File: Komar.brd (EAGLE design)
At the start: 58 x 58 mm, 108 parts, among them CON1 USB-VERTICAL, CON2 PINHEAD_1X01-2, CON3 CON-4P-TABS-STRAIGHT, CON4 CON-4P-TABS-STRAIGHT, CON5 CON-4P-TABS-STRAIGHT, CON6 CON-4P-TABS-STRAIGHT, CON7 CON-4P-TABS-STRAIGHT, CON8 CON-6P-SM06B, CON9 PINHEAD_1X01-2, IC1 TPD3S014DBVR-SOT23-6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

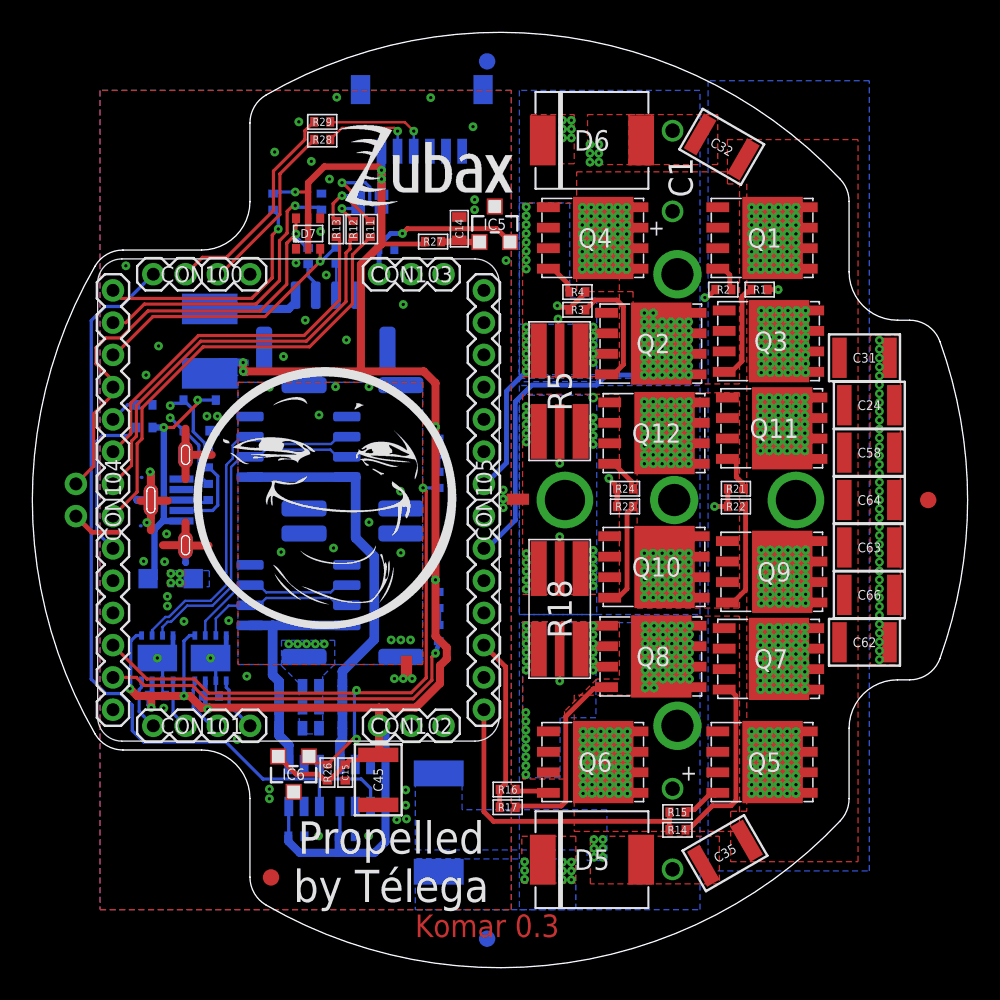
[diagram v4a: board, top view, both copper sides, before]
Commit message: CAN LEDs moved to other LEDs.
- DCP connector replaced with PLS-2 connector (marked DNM anyway)
- All LEDs moved 2 mm up
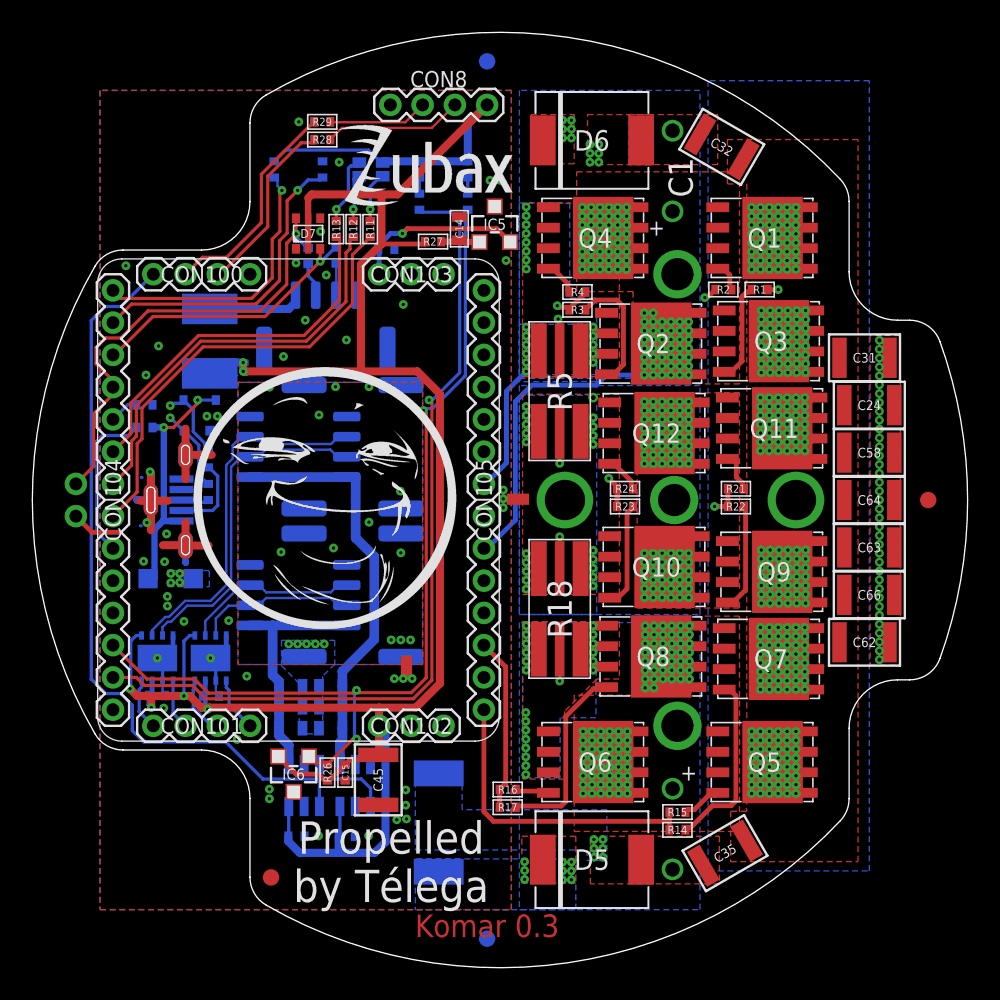
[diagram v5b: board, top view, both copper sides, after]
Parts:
- CON8: value CON-6P-SM06B -> PINHEAD_1X04-2; device Connectors:SM06B -> pinhead:1X04-PTH-2
- moved R9 26.8 mm to (24.0, 47.5)
- moved LED1 26.7 mm to (24.0, 49.5)
- moved R10 17.3 mm to (27.0, 47.5)
- moved LED2 17.3 mm to (27.0, 49.5)
- moved LED3 2.00 mm to (21.0, 49.5)
- moved LED4 2.00 mm to (18.0, 49.5)
- moved LED5 2.00 mm to (15.0, 49.5)
- moved CON8 1.21 mm to (25.2, 53.5), flipped to the top, turned to 0 degrees
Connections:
- net GND: now also CON8.1; no longer CON8.6, CON8.G1, CON8.G2
- net N$25: now also CON8.3; no longer CON8.2
- net N$26: now also CON8.2; no longer CON8.3
- net VDD_5V: now also CON8.4; no longer CON8.1
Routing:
- net CAN2_LED: track 23.4 -> 53.0 mm
- net CAN1_LED: track 41.0 -> 58.6 mm
- net VDD_5V: track 146.1 -> 161.6 mm, vias 15 -> 10
- net N$60: track 6.79 -> 3.17 mm
- net N$25: track 5.81 -> 8.62 mm, vias 1 -> 0
- net GAIN_OUT: track 15.1 -> 17.3 mm
- net N$58: track 2.94 -> 4.52 mm
- net GATE_ENABLE_OUT: track 18.3 -> 19.3 mm
- net N$59: track 2.06 -> 3.03 mm
- net N$26: track 6.66 -> 6.18 mm, vias 1 -> 0
- net GND: vias 50 -> 45

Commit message: Pins for lightpipes and capacitor support elements added
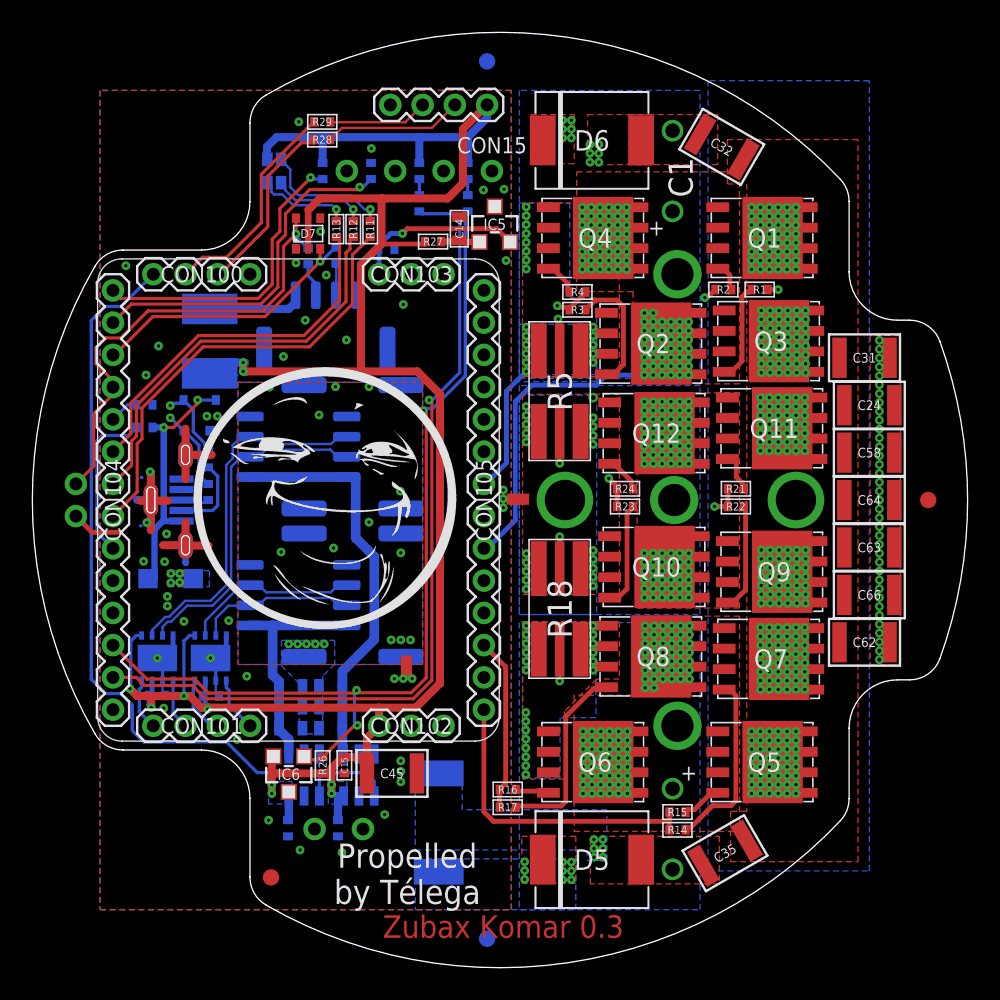
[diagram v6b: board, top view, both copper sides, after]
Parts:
- removed U$13: (no value), pixhawk_esc_1.5_master_lib:ZUBAX_LOGO_5X10
- added CON10, CON11, CON12, CON13, CON14, CON15: PINHEAD_1X01-2, pinhead:1X01-PTH-2
- moved LED3 6.00 mm to (15.0, 49.4), turned to 180 degrees
- moved LED4 3.00 mm to (21.0, 49.4)
- moved LED5 3.00 mm to (18.0, 49.4)
- moved C45 0.94 mm to (22.3, 12.1), turned to 0 degrees
- moved C3 0.74 mm to (18.9, 8.65), turned to 270 degrees
- moved C4 0.73 mm to (15.8, 8.65), turned to 270 degrees
- moved IC2 0.69 mm to (20.2, 11.9)
- moved IC1 0.65 mm to (16.9, 11.9)
- moved R26 0.54 mm to (18.0, 12.6)
- moved C15 0.45 mm to (19.4, 12.6)
- moved IC6 0.30 mm to (15.9, 12.0)
- moved LED1 0.10 mm to (24.0, 49.4)
- moved LED2 0.10 mm to (27.0, 49.4)
- moved R10 0.10 mm to (27.0, 47.4)
- moved R9 0.10 mm to (24.0, 47.4)
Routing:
- net VDD_5V: track 161.6 -> 155.4 mm, vias 10 -> 14
- net N$60: track 3.17 -> 8.21 mm
- net N$59: track 3.03 -> 6.00 mm
- net GATE_ENABLE_OUT: track 19.3 -> 22.3 mm
- net GAIN_OUT: track 17.3 -> 18.8 mm
- net N$58: track 4.52 -> 5.87 mm
- net CAN2_VDD: track 25.7 -> 25.1 mm
- net CAN1_VDD: track 15.0 -> 14.4 mm
- net GND: vias 45 -> 44
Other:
- board text added: "Zubax Komar 0.3"
- board text removed: "Komar 0.3"

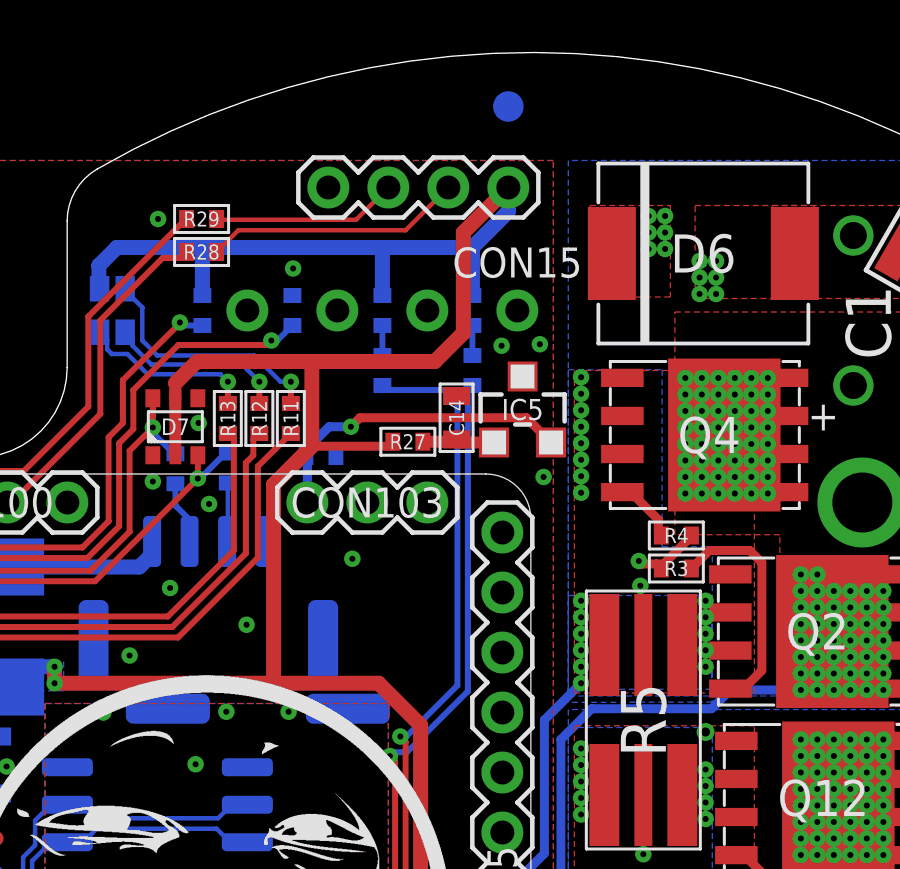
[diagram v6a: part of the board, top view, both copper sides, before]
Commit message: minor via adjustments
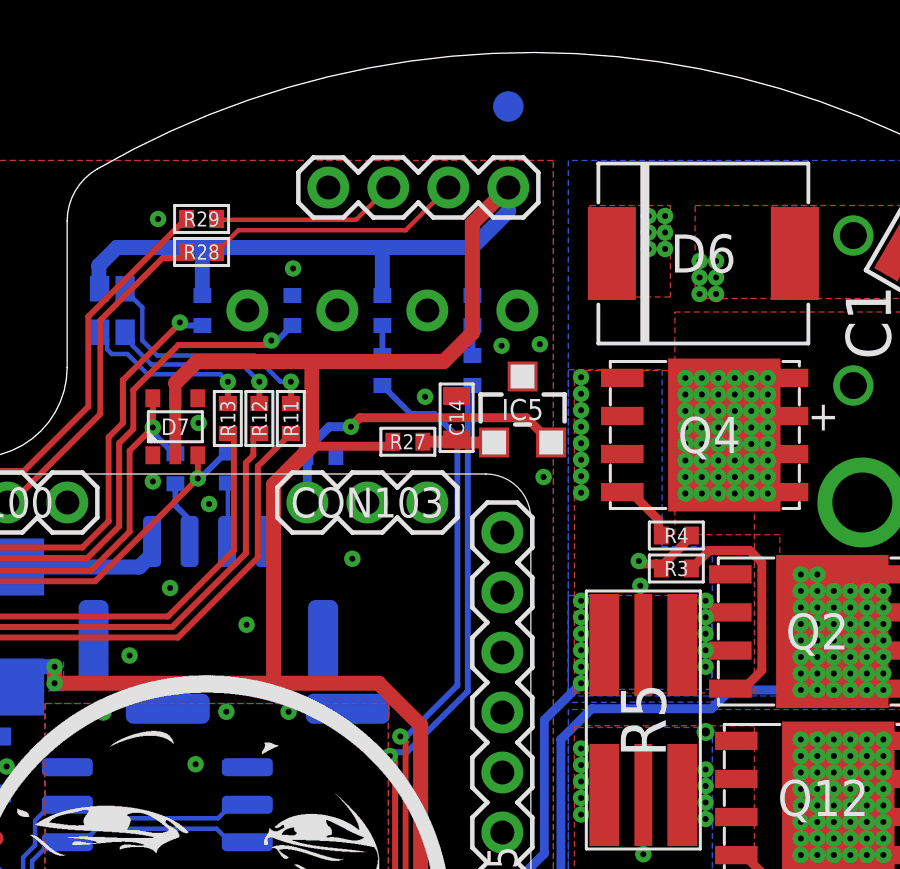
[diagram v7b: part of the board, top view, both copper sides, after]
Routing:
- net CAN2_LED: track 53.0 -> 52.3 mm
- net GND: vias 44 -> 45
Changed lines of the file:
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@@
 </layers>
 <board>
-<fusionsync huburn="a.cGVyc29uYWw6dWUyYWE4ZDY4" projecturn="a.cGVyc29uYWw6dWUyYWE4ZDY4IzIwMTgxMDI3MTU2OTA4Mjgx" f3durn="urn:adsk.wipprod:dm.lineage:yua-ROE5Tb29pIDQe9ePEg" pcbguid="" lastpulledtime="" lastsyncedchangeguid="" latestrevisionid="99d9bd0f-ab10-4f4c-9d53-7a49861b2582" lastsyncedrevisionid="99d9bd0f-ab10-4f4c-9d53-7a49861b2582" lastboardhashguid="794f6e2b-7879-ceef-8c4b-03a35c66539a" lastpushedtime="2020-05-13T06:42:24Z" linktopcb3d="%12"/>
+<fusionsync huburn="a.cGVyc29uYWw6dWUyYWE4ZDY4" projecturn="a.cGVyc29uYWw6dWUyYWE4ZDY4IzIwMTgxMDI3MTU2OTA4Mjgx" f3durn="urn:adsk.wipprod:dm.lineage:yua-ROE5Tb29pIDQe9ePEg" pcbguid="" lastpulledtime="" lastsyncedchangeguid="" latestrevisionid="bc640fca-ebd0-4133-9e78-bae0a64d3f22" lastsyncedrevisionid="bc640fca-ebd0-4133-9e78-bae0a64d3f22" lastboardhashguid="b37a2527-1958-626a-e22f-b3c5ef6fe3f5" lastpushedtime="2020-05-13T10:39:41Z" linktopcb3d="%12"/>
 <plain>
 <wire x1="29.2" y1="56.85" x2="29.2" y2="1.15" width="0.2" layer="22" style="shortdash"/>
@@
 <element name="CON13" library="pinhead" library_urn="urn:adsk.eagle:library:2540341" package="1X01-PTH-2" package3d_urn="urn:adsk.eagle:package:2540397/3" value="PINHEAD_1X01-2" x="17.5" y="8.6" smashed="yes"/>
 <element name="CON14" library="pinhead" library_urn="urn:adsk.eagle:library:2540341" package="1X01-PTH-2" package3d_urn="urn:adsk.eagle:package:2540397/3" value="PINHEAD_1X01-2" x="20.5" y="8.6" smashed="yes"/>
-<element name="CON15" library="pinhead" library_urn="urn:adsk.eagle:library:2540341" package="1X01-PTH-2" package3d_urn="urn:adsk.eagle:package:2540397/3" value="PINHEAD_1X01-2" x="28.5" y="49.4" smashed="yes">
-<attribute name="NAME" x="28.5" y="51" size="1" layer="25" font="vector" ratio="15" align="center"/>
-</element>
+<element name="CON15" library="pinhead" library_urn="urn:adsk.eagle:library:2540341" package="1X01-PTH-2" package3d_urn="urn:adsk.eagle:package:2540397/3" value="PINHEAD_1X01-2" x="28.5" y="49.4" smashed="yes"/>
 </elements>
 <signals>
@@
 <via x="21.85" y="9.5" extent="1-16" drill="0.2" diameter="0.55"/>
 <via x="16.6" y="7.3" extent="1-16" drill="0.2" diameter="0.55"/>
+<via x="25.425" y="46.525" extent="1-16" drill="0.2" diameter="0.55"/>
 <wire x1="9.5" y1="31.8" x2="9.5" y2="31.8" width="0" layer="19" extent="1-16"/>
 <wire x1="9.35" y1="31.8" x2="9.5" y2="31.8" width="0" layer="19" extent="1-1"/>
@@
 <wire x1="28.2" y1="52.7" x2="27" y2="51.5" width="0.5" layer="16"/>
 <wire x1="28.2" y1="52.7" x2="28.2" y2="53.5" width="0.5" layer="16"/>
-<wire x1="26.7" y1="52" x2="28.2" y2="53.5" width="0.5" layer="1"/>
-<wire x1="26.7" y1="52" x2="26.7" y2="48.65" width="0.5" layer="1"/>
-<wire x1="21.65" y1="47.7" x2="25.75" y2="47.7" width="0.5" layer="1"/>
-<wire x1="25.75" y1="47.7" x2="26.7" y2="48.65" width="0.5" layer="1"/>
+<wire x1="27" y1="52.3" x2="28.2" y2="53.5" width="0.5" layer="1"/>
+<wire x1="27" y1="52.3" x2="27" y2="48.65" width="0.5" layer="1"/>
+<wire x1="21.65" y1="47.7" x2="26.05" y2="47.7" width="0.5" layer="1"/>
+<wire x1="26.05" y1="47.7" x2="27" y2="48.65" width="0.5" layer="1"/>
 <wire x1="27" y1="49.9" x2="27" y2="51.5" width="0.5" layer="16"/>
 <wire x1="27" y1="51.5" x2="24" y2="51.5" width="0.5" layer="16"/>
@@
 <wire x1="26.5" y1="36.9" x2="24.8" y2="35.2" width="0.2" layer="16"/>
 <wire x1="24.6" y1="35.2" x2="24.8" y2="35.2" width="0.2" layer="16"/>
-<wire x1="26.5" y1="36.9" x2="26.5" y2="46.29350625" width="0.2" layer="16"/>
-<wire x1="26.04350625" y1="46.75" x2="24.15" y2="46.75" width="0.2" layer="16"/>
-<wire x1="24" y1="46.9" x2="24.15" y2="46.75" width="0.2" layer="16"/>
-<wire x1="26.5" y1="46.29350625" x2="26.04350625" y2="46.75" width="0.2" layer="16"/>
+<wire x1="26.5" y1="36.9" x2="26.5" y2="45.19350625" width="0.2" layer="16"/>
+<wire x1="25.74350625" y1="45.95" x2="24.95" y2="45.95" width="0.2" layer="16"/>
+<wire x1="24" y1="46.9" x2="24.95" y2="45.95" width="0.2" layer="16"/>
+<wire x1="26.5" y1="45.19350625" x2="25.74350625" y2="45.95" width="0.2" layer="16"/>
 </signal>
 <signal name="LED_BLUE">
